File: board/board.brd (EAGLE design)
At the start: 100 x 80 mm, 8 parts

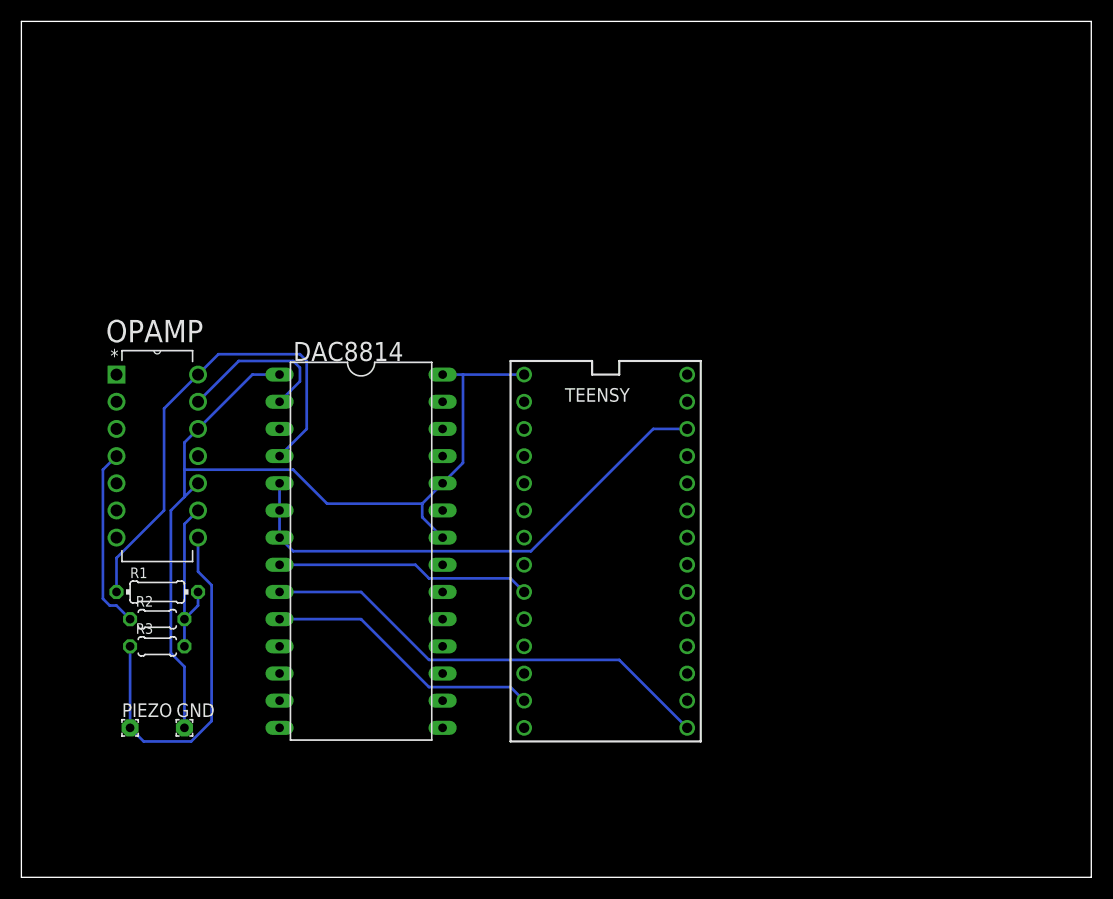
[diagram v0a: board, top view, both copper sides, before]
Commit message: Add missing connections
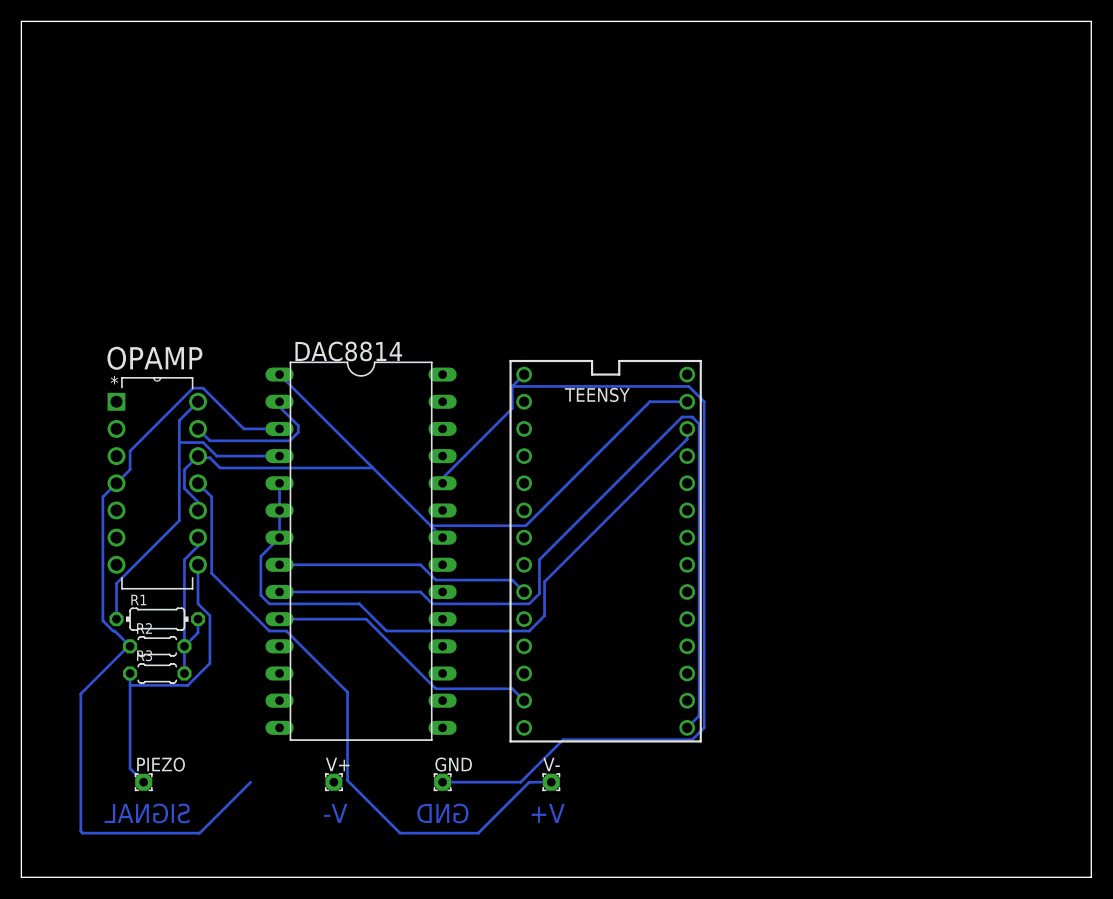
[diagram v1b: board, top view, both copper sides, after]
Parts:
- added V+, V-: (no value), wirepad:1,6/0,8
- moved GND 24.7 mm to (39.4, 8.89)
- moved PIEZO 5.24 mm to (11.4, 8.89)
- moved R1 2.54 mm to (12.7, 24.1)
- moved OPAMP 2.54 mm to (16.5, 29.2)
- moved R2 2.54 mm to (12.7, 21.6)
- moved R3 2.54 mm to (12.7, 19.1)
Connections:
- removed net VCC-: OPAMP.11
- new net V-: OPAMP.11, V-.1
- net AGND: now also DAC8814.1, DAC8814.22, OPAMP.10, OPAMP.12
- net GND: no longer DAC8814.1, DAC8814.22, DAC8814.28, OPAMP.10, OPAMP.12
- net V+: now also DAC8814.3, V+.1
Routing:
- net AGND: track 0.00 -> 73.3 mm
- net V+: track 17.2 -> 75.7 mm
- net V-: track 0.00 -> 57.6 mm
- net SCK: track 43.4 -> 77.9 mm
- net +3V3: track 48.4 -> 62.7 mm
- net RFBA: track 44.6 -> 33.4 mm
- net N$5: track 34.2 -> 28.7 mm
- net IOUTA: track 15.3 -> 13.7 mm
- net GND: track 89.8 -> 88.8 mm
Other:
- board text added: "GND"
- board text added: "SIGNAL"
- board text added: "V+"
- board text added: "V-"
